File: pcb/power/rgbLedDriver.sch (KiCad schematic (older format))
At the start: 39 parts, among them Q1 MMBT3904, Q2 MMBT3904, Q3 MMBT3904, Q4 MMBT3904, Q5 MMBT3904, Q6 MMBT3904, Q7 DMG2305UX, Q8 DMG2305UX, Q9 DMG2305UX

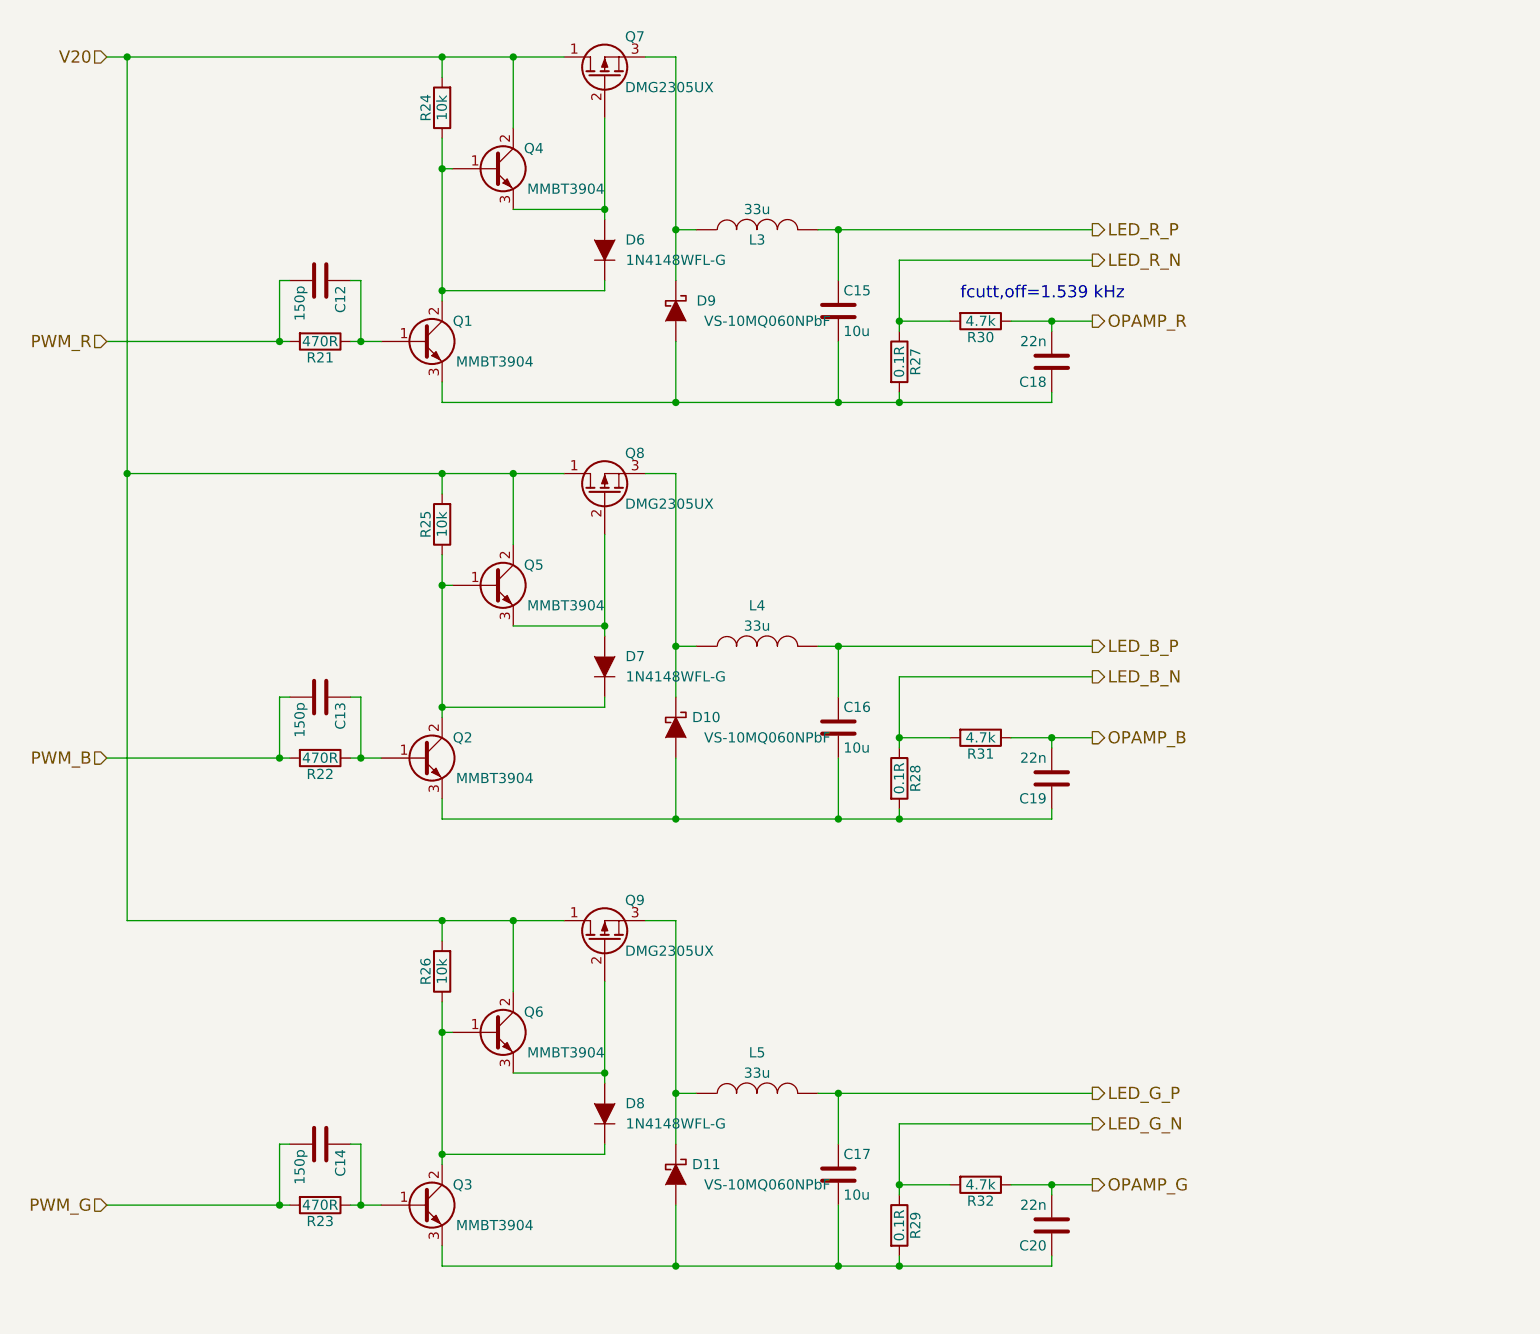
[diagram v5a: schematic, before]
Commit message: Checked all comp. of the LED Driver once more and assigned footprints.
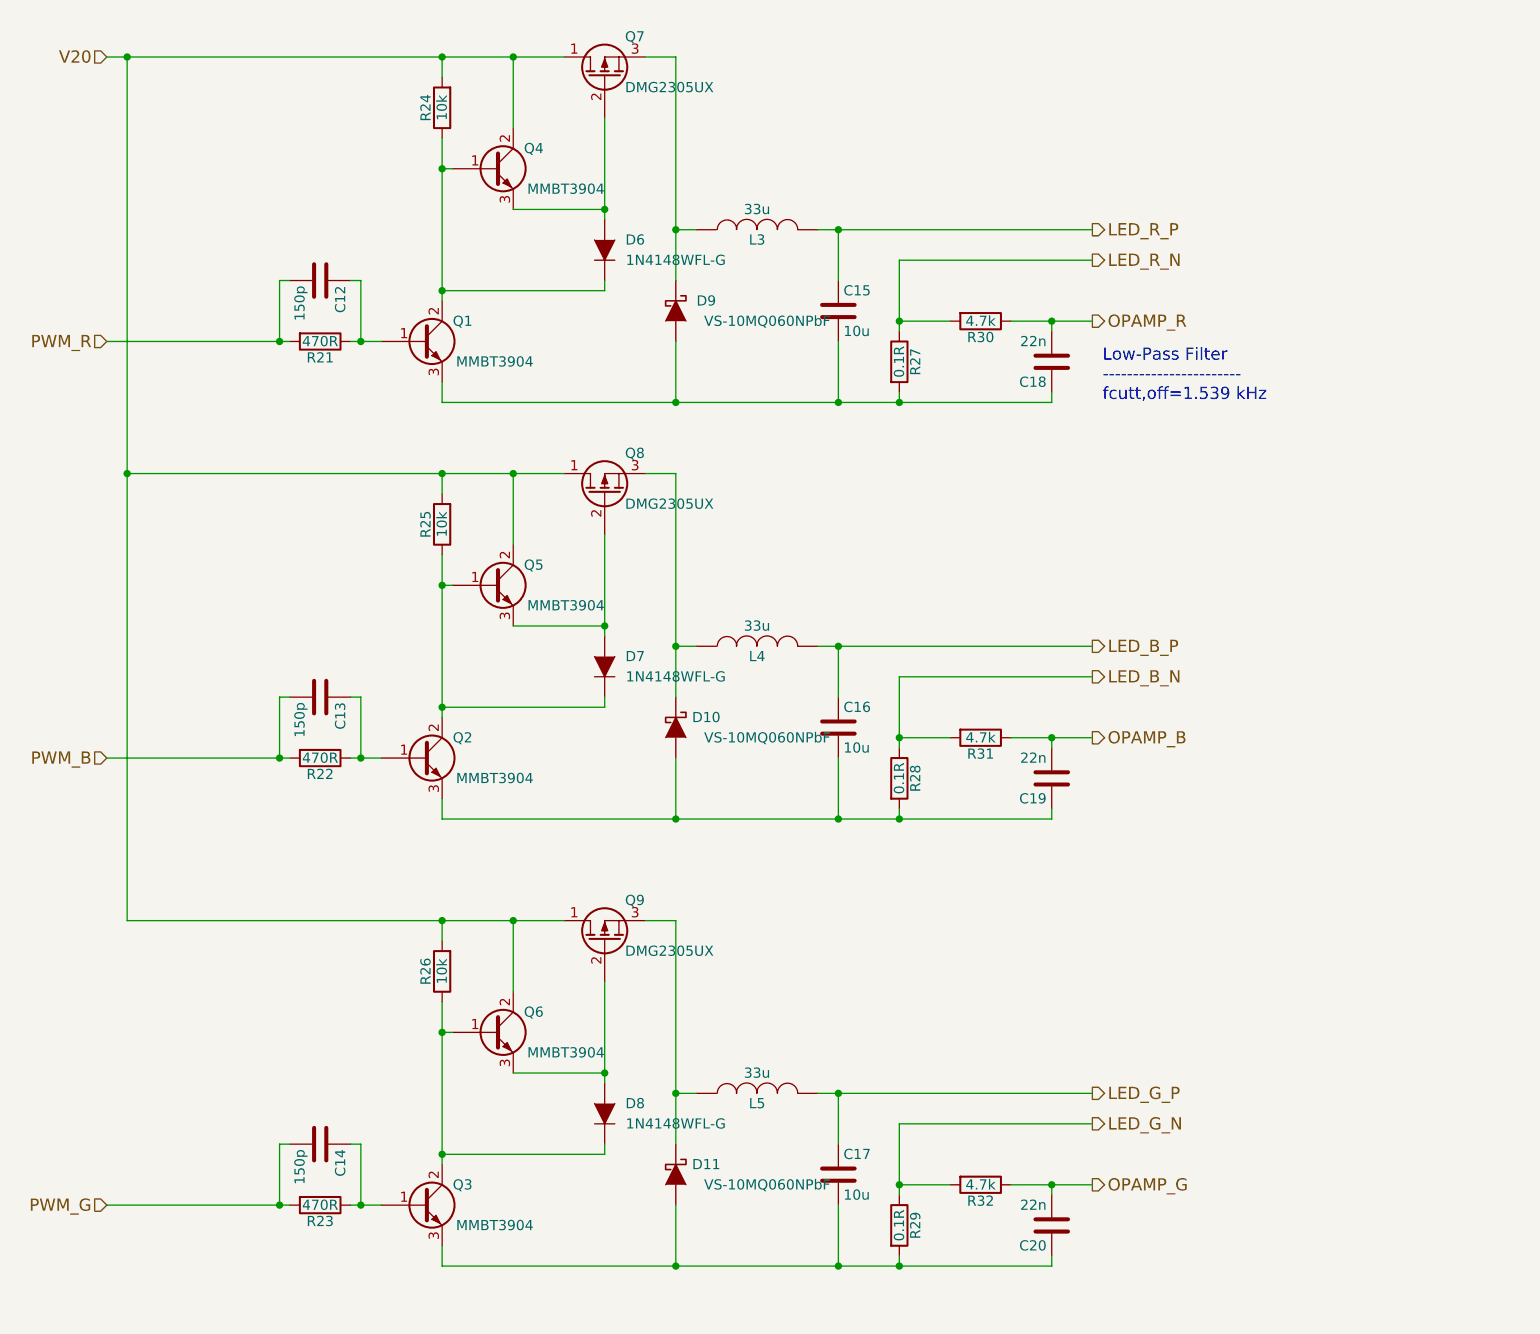
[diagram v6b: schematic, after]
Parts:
- C12, C13, C14: footprint (none) -> Capacitors_SMD:C_0603_HandSoldering; Digikey 490-3174-1-ND -> 399-1063-1-ND
- C15, C16, C17, C18, C19, C20, R27, R28, R29: footprint (none) -> Capacitors_SMD:C_0603_HandSoldering
- D10, D11, D9: footprint (none) -> Diodes_SMD:SMA_Handsoldering
- D6, D7, D8: footprint (none) -> Additional:SOD-123F
- L3, L4, L5: footprint (none) -> Additional:Bourns_SRN3015
- Q1, Q2, Q3, Q4, Q5, Q6, Q7, Q8, Q9: footprint (none) -> TO_SOT_Packages_SMD:SOT-23_Handsoldering
- R21, R22, R23, R24, R25, R26: footprint (none) -> Resistors_SMD:R_0603_HandSoldering
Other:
- note added: "Low-Pass Filter\n-----------------------\nfcutt,off=1.539 kHz"
- note removed: "fcutt,off=1.539 kHz"

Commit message: Added some more footprints. Maybe have to change some grounding stuff.
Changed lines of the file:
@@
 LED_G_N
 Wire Wire Line
-	1050 5350 2600 5350
-Wire Wire Line
-	2600 5350 2950 5350
-Wire Wire Line
-	2950 5350 3200 5350
+	1050 5350 3200 5350
 Wire Wire Line
 	2600 5450 2600 5350
 Connection ~ 2600 5350
 Wire Wire Line
-	2600 5750 2600 5900
-Wire Wire Line
-	2600 5900 2600 6500
-Wire Wire Line
-	2600 6500 2600 6550
+	2600 5750 2600 6550
 Wire Wire Line
 	2600 5900 2650 5900
@@
 	2950 6100 3400 6100
 Wire Wire Line
-	3400 5650 3400 6100
-Wire Wire Line
-	3400 6100 3400 6150
+	3400 5650 3400 6150
 Connection ~ 3400 6100
 Wire Wire Line
 	3400 6500 3400 6450
 Wire Wire Line
-	950  6750 1800 6750
-Wire Wire Line
-	1800 6750 1850 6750
-Wire Wire Line
-	2150 6750 2200 6750
-Wire Wire Line
-	2200 6750 2300 6750
+	950  6750 1850 6750
+Wire Wire Line
+	2150 6750 2300 6750
 Wire Wire Line
 	1850 6450 1800 6450
@@
 	3750 6750 3750 7050
 Wire Wire Line
-	2600 7050 3750 7050
-Wire Wire Line
-	3750 7050 4550 7050
-Wire Wire Line
-	4550 7050 4850 7050
-Wire Wire Line
-	4850 7050 5600 7050
+	2600 7050 5600 7050
 Wire Wire Line
 	2600 7050 2600 6950
@@
 	4850 7050 4850 7000
 Wire Wire Line
-	4450 6200 4550 6200
-Wire Wire Line
-	4550 6200 5800 6200
-Wire Wire Line
-	3750 5350 3750 6200
-Wire Wire Line
-	3750 6200 3750 6450
+	4450 6200 5800 6200
+Wire Wire Line
+	3750 5350 3750 6450
 Connection ~ 3750 6200
 Wire Wire Line
@@
 	5800 6350 4850 6350
 Wire Wire Line
-	4850 6350 4850 6650
-Wire Wire Line
-	4850 6650 4850 6700
+	4850 6350 4850 6700
 Wire Wire Line
 	5100 6650 4850 6650
 Connection ~ 4850 6650
 Wire Wire Line
-	5400 6650 5600 6650
-Wire Wire Line
-	5600 6650 5800 6650
+	5400 6650 5800 6650
 Wire Wire Line
 	5600 6650 5600 6700
@@
 LED_B_N
 Wire Wire Line
-	1050 3150 2600 3150
-Wire Wire Line
-	2600 3150 2950 3150
-Wire Wire Line
-	2950 3150 3200 3150
+	1050 3150 3200 3150
 Wire Wire Line
 	2600 3250 2600 3150
 Connection ~ 2600 3150
 Wire Wire Line
-	2600 3550 2600 3700
-Wire Wire Line
-	2600 3700 2600 4300
-Wire Wire Line
-	2600 4300 2600 4350
+	2600 3550 2600 4350
 Wire Wire Line
 	2600 3700 2650 3700
@@
 	2950 3900 3400 3900
 Wire Wire Line
-	3400 3450 3400 3900
-Wire Wire Line
-	3400 3900 3400 3950
+	3400 3450 3400 3950
 Connection ~ 3400 3900
 Wire Wire Line
 	3400 4300 3400 4250
 Wire Wire Line
-	950  4550 1800 4550
-Wire Wire Line
-	1800 4550 1850 4550
-Wire Wire Line
-	2150 4550 2200 4550
-Wire Wire Line
-	2200 4550 2300 4550
+	950  4550 1850 4550
+Wire Wire Line
+	2150 4550 2300 4550
 Wire Wire Line
 	1850 4250 1800 4250
@@
 	3750 4550 3750 4850
 Wire Wire Line
-	2600 4850 3750 4850
-Wire Wire Line
-	3750 4850 4550 4850
-Wire Wire Line
-	4550 4850 4850 4850
-Wire Wire Line
-	4850 4850 5600 4850
+	2600 4850 5600 4850
 Wire Wire Line
 	2600 4850 2600 4750
@@
 	4850 4850 4850 4800
 Wire Wire Line
-	4450 4000 4550 4000
-Wire Wire Line
-	4550 4000 5800 4000
-Wire Wire Line
-	3750 3150 3750 4000
-Wire Wire Line
-	3750 4000 3750 4250
+	4450 4000 5800 4000
+Wire Wire Line
+	3750 3150 3750 4250
 Connection ~ 3750 4000
 Wire Wire Line
@@
 	5800 4150 4850 4150
 Wire Wire Line
-	4850 4150 4850 4450
-Wire Wire Line
-	4850 4450 4850 4500
+	4850 4150 4850 4500
 Wire Wire Line
 	5100 4450 4850 4450
 Connection ~ 4850 4450
 Wire Wire Line
-	5400 4450 5600 4450
-Wire Wire Line
-	5600 4450 5800 4450
+	5400 4450 5800 4450
 Wire Wire Line
 	5600 4450 5600 4500
@@
 $EndComp
 Wire Wire Line
-	950  1100 1050 1100
-Wire Wire Line
-	1050 1100 2600 1100
-Wire Wire Line
-	2600 1100 2950 1100
-Wire Wire Line
-	2950 1100 3200 1100
+	950  1100 3200 1100
 Wire Wire Line
 	2600 1200 2600 1100
 Connection ~ 2600 1100
 Wire Wire Line
-	2600 1500 2600 1650
-Wire Wire Line
-	2600 1650 2600 2250
-Wire Wire Line
-	2600 2250 2600 2300
+	2600 1500 2600 2300
 Wire Wire Line
 	2600 1650 2650 1650
@@
 	2950 1850 3400 1850
 Wire Wire Line
-	3400 1400 3400 1850
-Wire Wire Line
-	3400 1850 3400 1900
+	3400 1400 3400 1900
 Connection ~ 3400 1850
 Wire Wire Line
 	3400 2250 3400 2200
 Wire Wire Line
-	950  2500 1800 2500
-Wire Wire Line
-	1800 2500 1850 2500
-Wire Wire Line
-	2150 2500 2200 2500
-Wire Wire Line
-	2200 2500 2300 2500
+	950  2500 1850 2500
+Wire Wire Line
+	2150 2500 2300 2500
 Wire Wire Line
 	1850 2200 1800 2200
@@
 	3750 2500 3750 2800
 Wire Wire Line
-	2600 2800 3750 2800
-Wire Wire Line
-	3750 2800 4550 2800
-Wire Wire Line
-	4550 2800 4850 2800
-Wire Wire Line
-	4850 2800 5600 2800
+	2600 2800 5600 2800
 Wire Wire Line
 	2600 2800 2600 2700
@@
 	4850 2800 4850 2750
 Wire Wire Line
-	4450 1950 4550 1950
-Wire Wire Line
-	4550 1950 5800 1950
-Wire Wire Line
-	3750 1100 3750 1950
-Wire Wire Line
-	3750 1950 3750 2200
+	4450 1950 5800 1950
+Wire Wire Line
+	3750 1100 3750 2200
 Connection ~ 3750 1950
 Wire Wire Line
@@
 	5800 2100 4850 2100
 Wire Wire Line
-	4850 2100 4850 2400
-Wire Wire Line
-	4850 2400 4850 2450
+	4850 2100 4850 2450
 Wire Wire Line
 	5100 2400 4850 2400
 Connection ~ 4850 2400
 Wire Wire Line
-	5400 2400 5600 2400
-Wire Wire Line
-	5600 2400 5800 2400
+	5400 2400 5800 2400
 Wire Wire Line
 	5600 2400 5600 2450
@@
 Connection ~ 1050 3150
 Wire Wire Line
-	1050 1100 1050 3150
-Wire Wire Line
-	1050 3150 1050 5350
+	1050 1100 1050 5350
 Text Notes 5850 2800 0    60   ~ 0
 Low-Pass Filter\n-----------------------\nfcutt,off=1.539 kHz

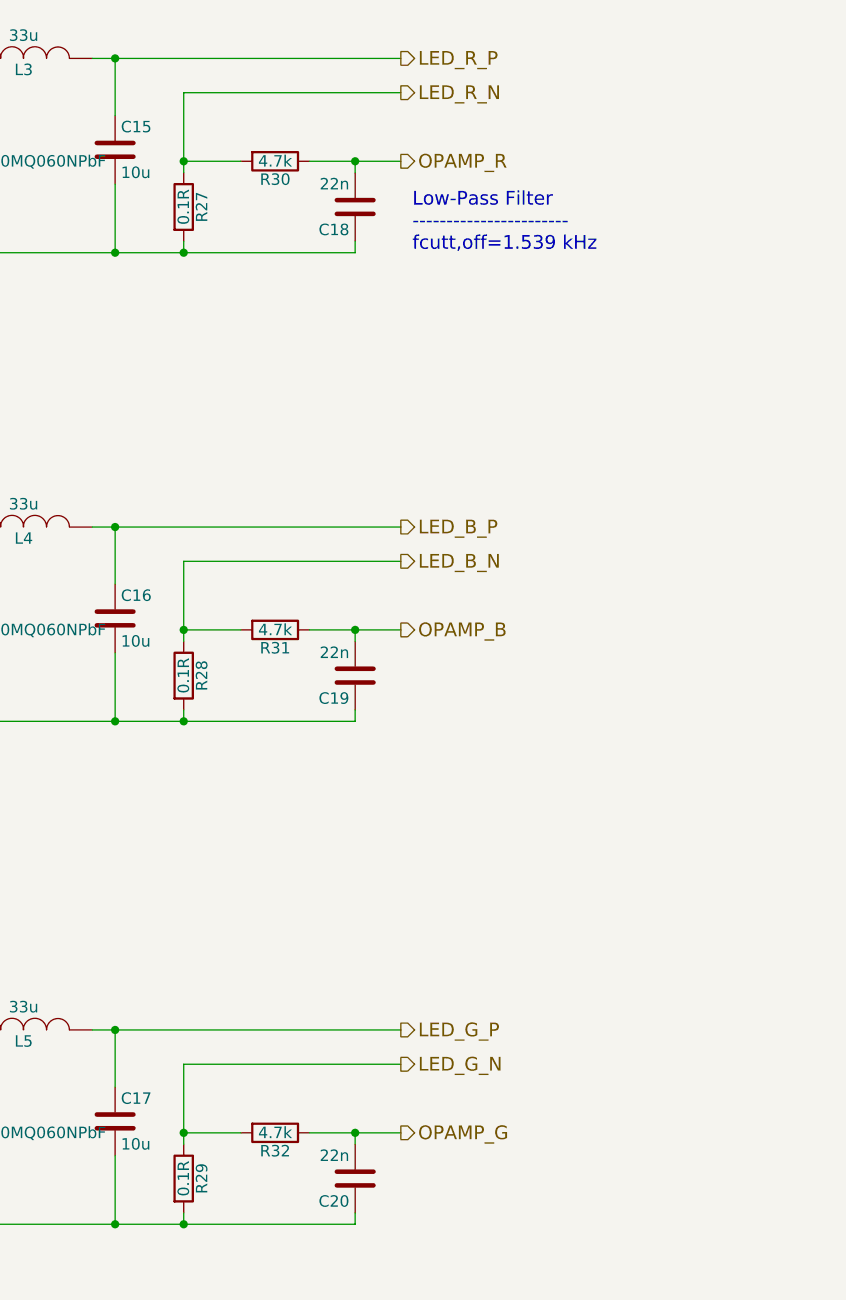
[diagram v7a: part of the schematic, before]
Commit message: All footprints assigned. No DRC errors anymore.
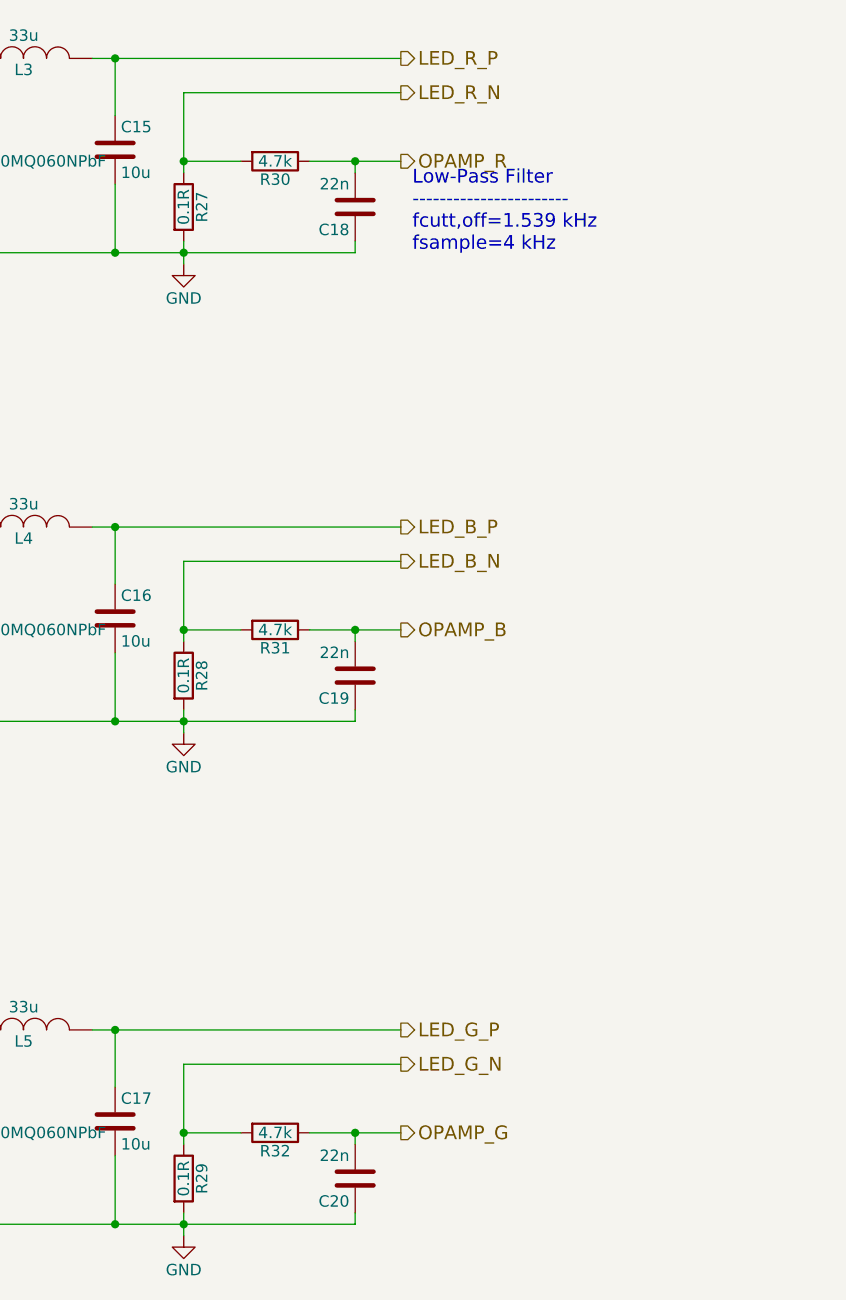
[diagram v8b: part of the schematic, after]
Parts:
- R30, R31, R32: footprint (none) -> Resistors_SMD:R_0603_HandSoldering
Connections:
- net GND: now reaches C15.2, C18.1, D9.2 (A), Q1.3 (E), R27.2
- net GND: now also C16.2, C17.2, C19.1, C20.1, D10.2 (A), D11.2 (A), Q2.3 (E), Q3.3 (E), R28.2, R29.2
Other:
- note added: "Low-Pass Filter\n-----------------------\nfcutt,off=1.539 kHz\nfsample=4 kHz"
- note removed: "Low-Pass Filter\n-----------------------\nfcutt,off=1.539 kHz"
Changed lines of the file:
@@
 Connection ~ 4550 7050
 Wire Wire Line
-	4850 7050 4850 7000
+	4850 7000 4850 7100
 Wire Wire Line
 	4450 6200 5800 6200
@@
 Connection ~ 4550 4850
 Wire Wire Line
-	4850 4850 4850 4800
+	4850 4800 4850 4900
 Wire Wire Line
 	4450 4000 5800 4000
@@
 F 0 "R30" V 5330 2400 50  0000 C CNN
 F 1 "4.7k" V 5250 2400 50  0000 C CNN
-F 2 "" V 5180 2400 50  0000 C CNN
+F 2 "Resistors_SMD:R_0603_HandSoldering" V 5180 2400 50  0001 C CNN
 F 3 "http://www.yageo.com.tw/exep/pages/download/literatures/PYu-R_INT-thick_7.pdf" H 5250 2400 50  0001 C CNN
 F 4 "311-4.7KGRCT-ND" V 5250 2400 60  0001 C CNN "Digikey"
@@
 Connection ~ 4550 2800
 Wire Wire Line
-	4850 2800 4850 2750
+	4850 2750 4850 2850
 Wire Wire Line
 	4450 1950 5800 1950
@@
 	1050 1100 1050 5350
 Text Notes 5850 2800 0    60   ~ 0
-Low-Pass Filter\n-----------------------\nfcutt,off=1.539 kHz
+Low-Pass Filter\n-----------------------\nfcutt,off=1.539 kHz\nfsample=4 kHz
 $Comp
 L D D6
@@
 F 0 "R32" V 5330 6650 50  0000 C CNN
 F 1 "4.7k" V 5250 6650 50  0000 C CNN
-F 2 "" V 5180 6650 50  0000 C CNN
+F 2 "Resistors_SMD:R_0603_HandSoldering" V 5180 6650 50  0001 C CNN
 F 3 "http://www.yageo.com.tw/exep/pages/download/literatures/PYu-R_INT-thick_7.pdf" H 5250 6650 50  0001 C CNN
 F 4 "311-4.7KGRCT-ND" V 5250 6650 60  0001 C CNN "Digikey"
@@
 F 0 "R31" V 5330 4450 50  0000 C CNN
 F 1 "4.7k" V 5250 4450 50  0000 C CNN
-F 2 "" V 5180 4450 50  0000 C CNN
+F 2 "Resistors_SMD:R_0603_HandSoldering" V 5180 4450 50  0001 C CNN
 F 3 "http://www.yageo.com.tw/exep/pages/download/literatures/PYu-R_INT-thick_7.pdf" H 5250 4450 50  0001 C CNN
 F 4 "311-4.7KGRCT-ND" V 5250 4450 60  0001 C CNN "Digikey"
@@
 	-1   0    0    1
 $EndComp
+$Comp
+L GND #PWR020
+U 1 1 584185EC
+P 4850 2850
+F 0 "#PWR020" H 4850 2600 50  0001 C CNN
+F 1 "GND" H 4850 2700 50  0000 C CNN
+F 2 "" H 4850 2850 50  0000 C CNN
+F 3 "" H 4850 2850 50  0000 C CNN
+	1    4850 2850
+	1    0    0    -1
+$EndComp
+$Comp
+L GND #PWR021
+U 1 1 584188BC
+P 4850 7100
+F 0 "#PWR021" H 4850 6850 50  0001 C CNN
+F 1 "GND" H 4850 6950 50  0000 C CNN
+F 2 "" H 4850 7100 50  0000 C CNN
+F 3 "" H 4850 7100 50  0000 C CNN
+	1    4850 7100
+	1    0    0    -1
+$EndComp
+$Comp
+L GND #PWR022
+U 1 1 58418AC2
+P 4850 4900
+F 0 "#PWR022" H 4850 4650 50  0001 C CNN
+F 1 "GND" H 4850 4750 50  0000 C CNN
+F 2 "" H 4850 4900 50  0000 C CNN
+F 3 "" H 4850 4900 50  0000 C CNN
+	1    4850 4900
+	1    0    0    -1
+$EndComp
 $EndSCHEMATC
